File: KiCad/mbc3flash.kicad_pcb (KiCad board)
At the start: 2 copper layers, 51.1 x 61.3 mm, 18 parts, among them M1 FM18W08, U0 CartBus, U1 MBC3, U2 BA6129AF, U3 74LVC1G332GW,125, U4 AM29F016, Y1 Crystal

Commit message: Update mbc3flash.kicad_pcb
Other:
- board text added: "Rev 1.4.1"
- board text removed: "Rev 1.4.2"
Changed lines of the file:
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@@
   (gr_circle (center 127 90.678) (end 127.508 90.932) (layer F.SilkS) (width 0.2))
   (gr_line (start 117.389992 72.6) (end 167.88 72.6) (layer F.SilkS) (width 0.2))
-  (gr_text "Rev 1.4.2" (at 157.934 70.612) (layer B.Mask)
+  (gr_text "Rev 1.4.1" (at 157.934 70.612) (layer B.Mask)
     (effects (font (size 1.5 1.5) (thickness 0.3)) (justify mirror))
   )

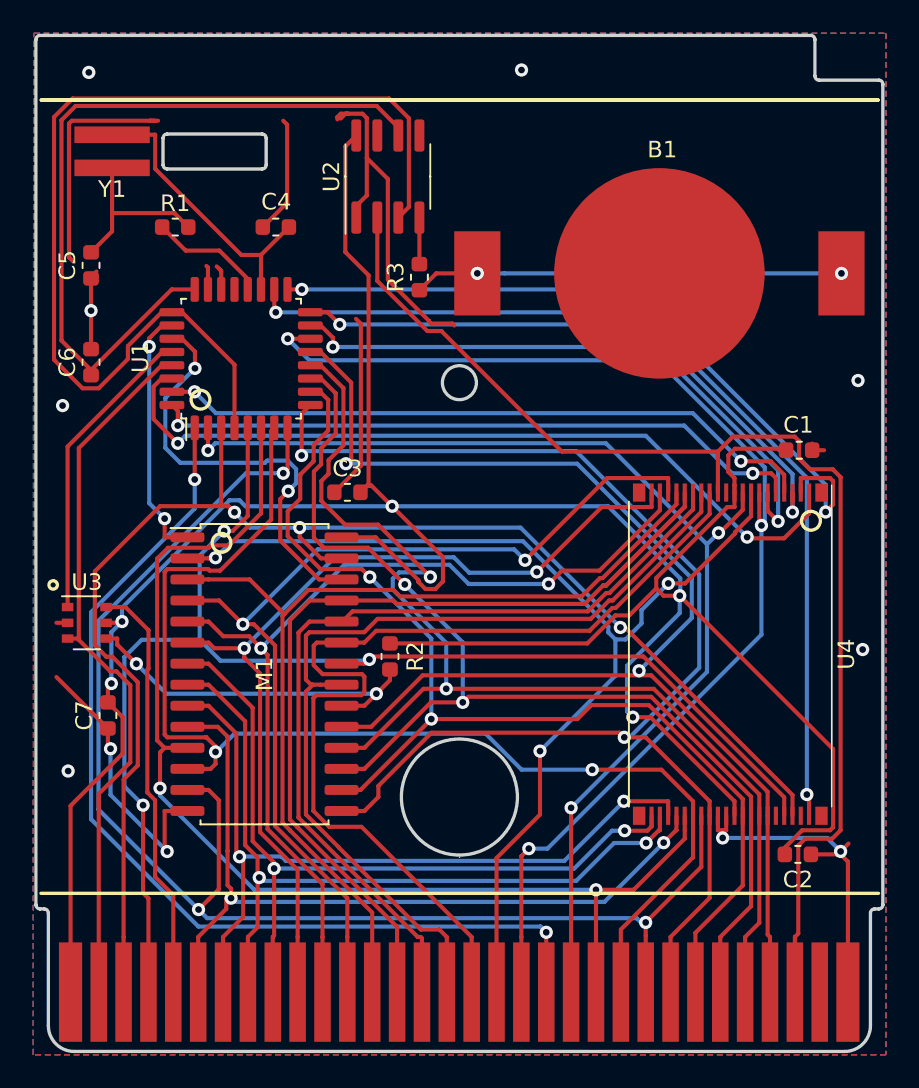
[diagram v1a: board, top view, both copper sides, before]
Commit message: Release 1.5
- Updated kicad version from 5 to 6.0
- Redrew outline to be a closer match to original
- Added markings to make cart look more original
- Added switch for 2x2mb mode (this means the cart can store 2 separate roms, saves are still shared)
- Changed footprint designators
- Added test pads
- Added date marking
- Relocated alignment holes for a better fit
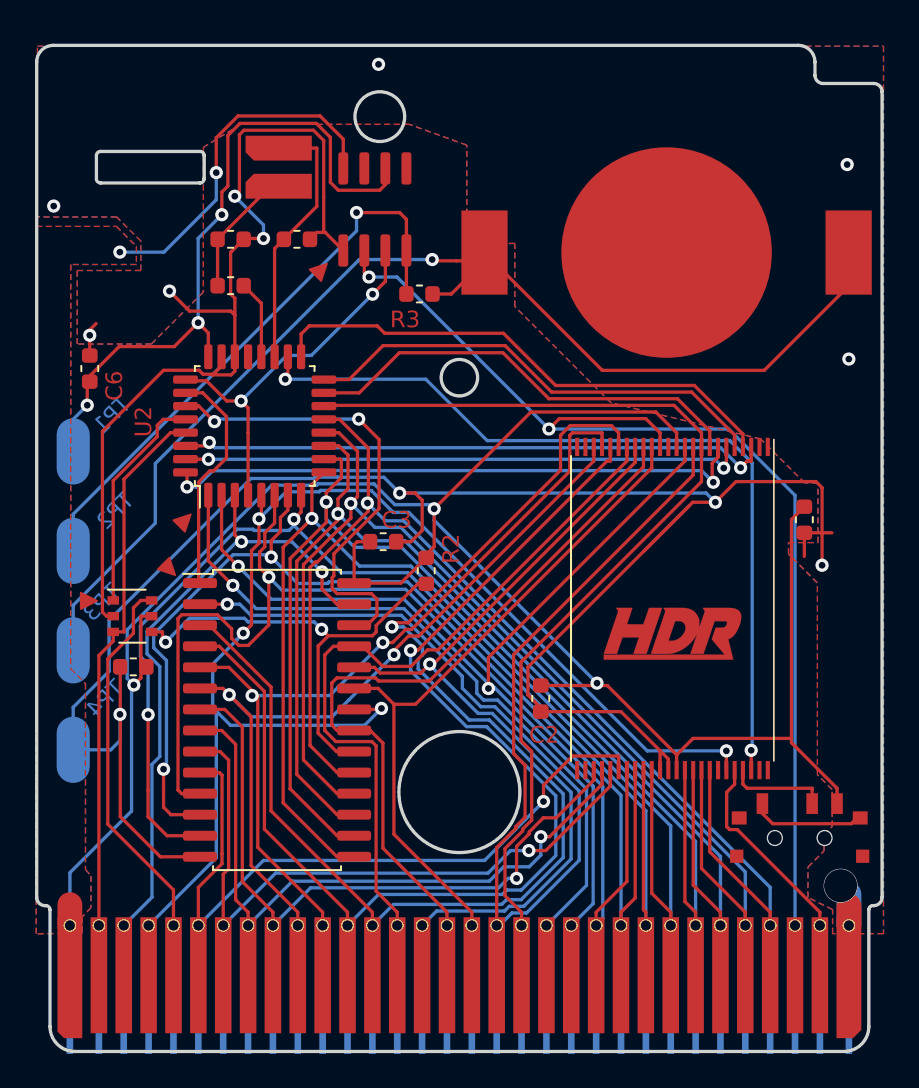
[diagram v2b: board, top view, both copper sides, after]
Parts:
- added G***: LOGO, Custom:HDR_Logo_Tiny, F.Cu at (155.5, 104.8)
- added GNDPAD1: Nintendo_3x3_GNDPad, Custom:Nintendo_3x3_GNDPad, F.Cu at (120.1, 72.3)
- added PAD*: GBA-ProductionIndicator, Custom:GBA-ProductionIndicator, B.Cu at (153.3, 82.3)
- added REF**: OSHW-Logo_5.7x6mm_Copper, Symbol:OSHW-Logo_5.7x6mm_Copper, B.Cu at (160.5, 86.8)
- added SW1: SW_SPDT, Custom:SW_SPDT-K3-1296S-E1, F.Cu at (163.2, 117.1)
- added TP1: RTC_VOUT, Custom:GameBoy_Testpoint, B.Cu at (119.3, 93.8)
- added TP2: Battery_Positive_After_Resistor, Custom:GameBoy_Testpoint, B.Cu at (119.3, 99.8)
- added TP3: Battery_Positive, Custom:GameBoy_Testpoint, B.Cu at (119.3, 105.8)
- added TP4: Ground, Custom:GameBoy_Testpoint, B.Cu at (119.3, 111.8)
- U0: footprint NintendoFootprints:CartBus -> Connector_GameBoy:GameBoy_GamePak_CGB-002_P1.50mm_Edge
- U1: renamed from U4; footprint Custom:AM29F0XX -> Package_SO:TSOP-I-48_18.4x12mm_P0.5mm
- moved U0 25.0 mm to (142.6, 130.0)
- moved C2 18.1 mm to (147.5, 108.7), turned to -90 degrees
- moved Y1 10.1 mm to (131.7, 76.7)
- moved C5 8.57 mm to (128.8, 81.0), turned to 180 degrees
- moved R2 5.61 mm to (140.6, 101.0)
- moved R1 4.87 mm to (128.8, 83.8), turned to 180 degrees
- moved U1 4.45 mm to (155.5, 103.3)
- moved C1 4.21 mm to (163.4, 97.9), turned to 90 degrees
- moved U2 4.15 mm to (130.6, 92.0)
- moved C3 3.68 mm to (138.0, 99.2), turned to 180 degrees
- moved C7 3.31 mm to (122.9, 106.8), turned to 0 degrees
- moved U3 2.87 mm to (131.6, 110.0)
- moved U5 2.78 mm to (122.9, 103.7)
- moved U4 2.14 mm to (137.5, 79.2)
- moved C4 1.47 mm to (132.8, 81.0), turned to 0 degrees
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- renumbered U1 to U2, M1 to U3, U2 to U4, U3 to U5
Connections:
- net Net-(B1-Pad1) renamed BT+
- net Net-(R3-Pad2) renamed Vbatt
- U0 pad 31: Net-(U0-Pad31) -> WE_AUD
- U1 pad 44: \WR -> WE_AUD
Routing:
- net GND: track 106.5 -> 196.7 mm, vias 11 -> 13
- net \WR: track 87.6 -> 38.8 mm, vias 3 -> 2
- net BT+: track 25.9 -> 71.6 mm, vias 2 -> 1
- net \RST: track 62.3 -> 23.3 mm, vias 0 -> 2
- net Vbatt: track 2.81 -> 35.2 mm, vias 0 -> 1
- net VCC: track 176.2 -> 152.8 mm
- net A11: track 60.0 -> 40.8 mm
- net A14: track 60.1 -> 42.1 mm, vias 2 -> 1
- net A7: track 59.3 -> 76.9 mm, vias 0 -> 1
- net A8: track 59.8 -> 44.7 mm
- net A13: track 73.8 -> 59.1 mm, vias 3 -> 0
- net RA18: track 43.9 -> 31.7 mm, vias 2 -> 0
- net RA19: track 48.0 -> 35.9 mm
- net WE_AUD: track 0.00 -> 12.2 mm
- net D2: track 86.2 -> 74.3 mm, vias 3 -> 2
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- added copper zone on B.Cu, net VCC
- added copper zone on F.Cu, net VCC
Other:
- board size 51.1 x 61.3 mm -> 51 x 60.7 mm
- net class Default removed
- board text added: "'21"
- board text added: "1"
- board text added: "1 5"
- board text added: "12"
- board text added: "2021 HDR"
- board text added: "6"
- board text added: "7"
- board text added: "Batt CR2025"
- board text added: "C1"
- board text added: "C2"
- board text added: "C3"
- board text added: "C4"
- board text added: "C5"
- board text added: "C6"
- board text added: "C7"
- board text added: "MBC-FLSH-3"
- board text added: "MBC3"
- board text added: "R1"
- board text added: "R2"
- board text added: "R3"
- board text added: "TP1"
- board text added: "TP2"
- board text added: "TP3"
- board text added: "TP4"
- board text added: "U1"
- board text added: "U2"
- board text added: "U3"
- board text added: "U4"
- board text added: "U5"
- board text added: "X1"
- board text removed: "Rev 1.4.1"
